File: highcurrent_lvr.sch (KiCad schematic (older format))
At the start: 6 parts

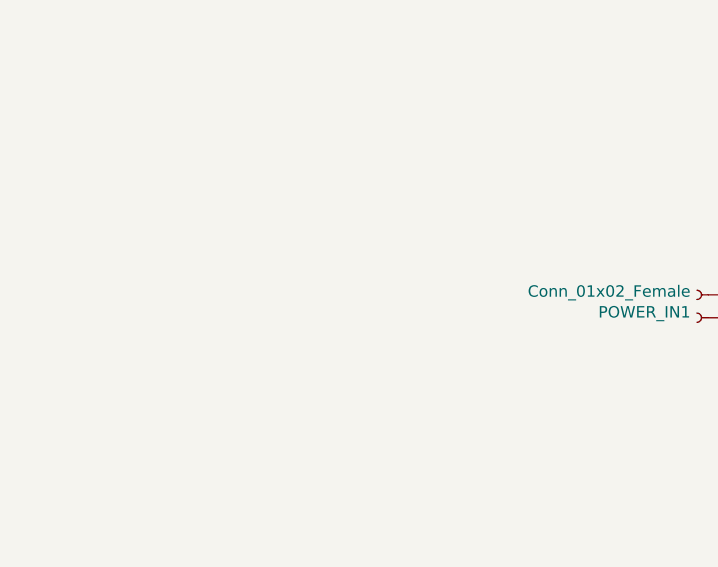
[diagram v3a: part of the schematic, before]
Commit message: added panelization
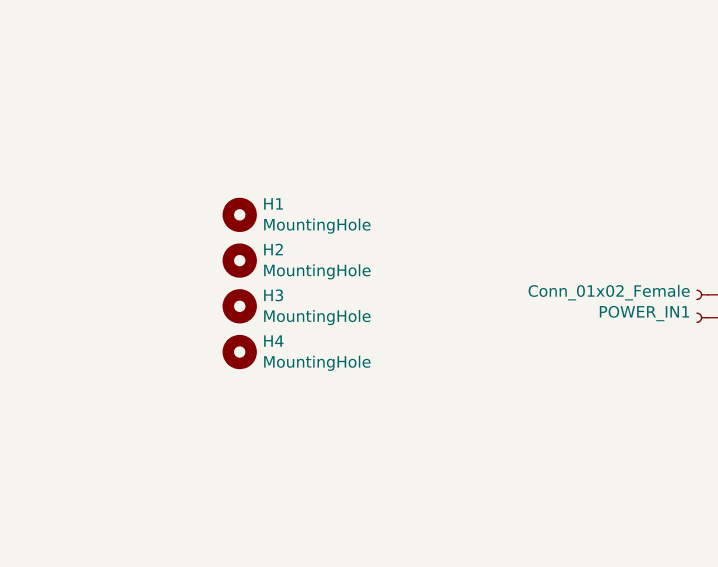
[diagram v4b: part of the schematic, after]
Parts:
- added H1, H2, H3, H4: MountingHole, MountingHole:MountingHole_4mm, symbol Mechanical:MountingHole
- POWER_IN1, POWER_OUT1: dk_pn 277-1258-ND -> (none); ms_pn 651-1711026 -> (none)
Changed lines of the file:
@@
 Text Notes 3750 4600 0    50   ~ 0
 add reverse polarity protection
-$Comp
-L Connector:Conn_01x02_Female POWER_IN1
-U 1 1 602E4815
-P 3550 3250
-F 0 "POWER_IN1" H 3578 3226 50  0000 L CNN
-F 1 "Conn_01x02_Female" H 3578 3135 50  0000 L CNN
-F 2 "wire-connector-lib:connector-wire-3cm2-2pin-smd" H 3550 3250 50  0001 C CNN
-F 3 "~" H 3550 3250 50  0001 C CNN
-F 4 "651-1711026" H 3550 3250 50  0001 C CNN "ms_pn"
-F 5 "277-1258-ND" H 3550 3250 50  0001 C CNN "dk_pn"
-	1    3550 3250
-	-1   0    0    1
-$EndComp
-$Comp
-L Connector:Conn_01x02_Female POWER_OUT1
-U 1 1 602E8D12
-P 8150 3250
-F 0 "POWER_OUT1" H 8178 3226 50  0000 L CNN
-F 1 "Conn_01x02_Female" H 8178 3135 50  0000 L CNN
-F 2 "wire-connector-lib:connector-wire-3cm2-2pin-smd" H 8150 3250 50  0001 C CNN
-F 3 "~" H 8150 3250 50  0001 C CNN
-F 4 "651-1711026" H 8150 3250 50  0001 C CNN "ms_pn"
-F 5 "277-1258-ND" H 8150 3250 50  0001 C CNN "dk_pn"
-	1    8150 3250
-	1    0    0    1
-$EndComp
-$Comp
-L Device:LED D1
-U 1 1 60393075
-P 7250 4150
-F 0 "D1" V 7289 4032 50  0000 R CNN
-F 1 "LED" V 7198 4032 50  0000 R CNN
-F 2 "LED_SMD:LED_0805_2012Metric_Pad1.15x1.40mm_HandSolder" H 7250 4150 50  0001 C CNN
-F 3 "~" H 7250 4150 50  0001 C CNN
-F 4 "754-2044-1-ND" H 7250 4150 50  0001 C CNN "dk_pn"
-F 5 "604-APTD2012LSURCK" H 7250 4150 50  0001 C CNN "ms_pn"
-	1    7250 4150
-	0    -1   -1   0
-$EndComp
 Wire Wire Line
 	7250 3450 7250 4000
-$Comp
-L Device:R R7
-U 1 1 603954F6
-P 7250 4600
-F 0 "R7" H 7320 4646 50  0000 L CNN
-F 1 "1k8" H 7320 4555 50  0000 L CNN
-F 2 "Resistor_SMD:R_0805_2012Metric_Pad1.20x1.40mm_HandSolder" V 7180 4600 50  0001 C CNN
-F 3 "~" H 7250 4600 50  0001 C CNN
-F 4 "541-10510-1-ND" H 7250 4600 50  0001 C CNN "dk_pn"
-F 5 "71-RCS08051K80FKEA" H 7250 4600 50  0001 C CNN "ms_pn"
-	1    7250 4600
-	1    0    0    -1
-$EndComp
 $Comp
 L power:GND #PWR0108
@@
 Wire Wire Line
 	7250 4450 7250 4300
-$Comp
-L Device:LED D2
-U 1 1 603BAE9B
-P 5450 4100
-F 0 "D2" V 5489 3982 50  0000 R CNN
-F 1 "LED" V 5398 3982 50  0000 R CNN
-F 2 "LED_SMD:LED_0805_2012Metric_Pad1.15x1.40mm_HandSolder" H 5450 4100 50  0001 C CNN
-F 3 "~" H 5450 4100 50  0001 C CNN
-F 4 "754-2044-1-ND" H 5450 4100 50  0001 C CNN "dk_pn"
-F 5 "604-APTD2012LSURCK" H 5450 4100 50  0001 C CNN "ms_pn"
-	1    5450 4100
-	0    -1   -1   0
-$EndComp
-$Comp
-L Device:R R6
-U 1 1 603BAEA3
-P 5450 4550
-F 0 "R6" H 5520 4596 50  0000 L CNN
-F 1 "1k8" H 5520 4505 50  0000 L CNN
-F 2 "Resistor_SMD:R_0805_2012Metric_Pad1.20x1.40mm_HandSolder" V 5380 4550 50  0001 C CNN
-F 3 "~" H 5450 4550 50  0001 C CNN
-F 4 "541-10510-1-ND" H 5450 4550 50  0001 C CNN "dk_pn"
-F 5 "71-RCS08051K80FKEA" H 5450 4550 50  0001 C CNN "ms_pn"
-	1    5450 4550
-	1    0    0    -1
-$EndComp
 $Comp
 L power:GND #PWR0114
@@
 Wire Wire Line
 	7100 3150 7950 3150
+$Comp
+L Device:R R6
+U 1 1 603BAEA3
+P 5450 4550
+F 0 "R6" H 5520 4596 50  0000 L CNN
+F 1 "1k8" H 5520 4505 50  0000 L CNN
+F 2 "Resistor_SMD:R_0805_2012Metric_Pad1.20x1.40mm_HandSolder" V 5380 4550 50  0001 C CNN
+F 3 "~" H 5450 4550 50  0001 C CNN
+F 4 "541-10510-1-ND" H 5450 4550 50  0001 C CNN "dk_pn"
+F 5 "71-RCS08051K80FKEA" H 5450 4550 50  0001 C CNN "ms_pn"
+	1    5450 4550
+	1    0    0    -1
+$EndComp
+$Comp
+L Device:LED D2
+U 1 1 603BAE9B
+P 5450 4100
+F 0 "D2" V 5489 3982 50  0000 R CNN
+F 1 "LED" V 5398 3982 50  0000 R CNN
+F 2 "LED_SMD:LED_0805_2012Metric_Pad1.15x1.40mm_HandSolder" H 5450 4100 50  0001 C CNN
+F 3 "~" H 5450 4100 50  0001 C CNN
+F 4 "754-2044-1-ND" H 5450 4100 50  0001 C CNN "dk_pn"
+F 5 "604-APTD2012LSURCK" H 5450 4100 50  0001 C CNN "ms_pn"
+	1    5450 4100
+	0    -1   -1   0
+$EndComp
+$Comp
+L Device:R R7
+U 1 1 603954F6
+P 7250 4600
+F 0 "R7" H 7320 4646 50  0000 L CNN
+F 1 "1k8" H 7320 4555 50  0000 L CNN
+F 2 "Resistor_SMD:R_0805_2012Metric_Pad1.20x1.40mm_HandSolder" V 7180 4600 50  0001 C CNN
+F 3 "~" H 7250 4600 50  0001 C CNN
+F 4 "541-10510-1-ND" H 7250 4600 50  0001 C CNN "dk_pn"
+F 5 "71-RCS08051K80FKEA" H 7250 4600 50  0001 C CNN "ms_pn"
+	1    7250 4600
+	1    0    0    -1
+$EndComp
+$Comp
+L Device:LED D1
+U 1 1 60393075
+P 7250 4150
+F 0 "D1" V 7289 4032 50  0000 R CNN
+F 1 "LED" V 7198 4032 50  0000 R CNN
+F 2 "LED_SMD:LED_0805_2012Metric_Pad1.15x1.40mm_HandSolder" H 7250 4150 50  0001 C CNN
+F 3 "~" H 7250 4150 50  0001 C CNN
+F 4 "754-2044-1-ND" H 7250 4150 50  0001 C CNN "dk_pn"
+F 5 "604-APTD2012LSURCK" H 7250 4150 50  0001 C CNN "ms_pn"
+	1    7250 4150
+	0    -1   -1   0
+$EndComp
+$Comp
+L Connector:Conn_01x02_Female POWER_OUT1
+U 1 1 602E8D12
+P 8150 3250
+F 0 "POWER_OUT1" H 8178 3226 50  0000 L CNN
+F 1 "Conn_01x02_Female" H 8178 3135 50  0000 L CNN
+F 2 "wire-connector-lib:connector-wire-3cm2-2pin-smd" H 8150 3250 50  0001 C CNN
+F 3 "~" H 8150 3250 50  0001 C CNN
+F 4 "" H 8150 3250 50  0001 C CNN "ms_pn"
+F 5 "" H 8150 3250 50  0001 C CNN "dk_pn"
+	1    8150 3250
+	1    0    0    1
+$EndComp
+$Comp
+L Connector:Conn_01x02_Female POWER_IN1
+U 1 1 602E4815
+P 3550 3250
+F 0 "POWER_IN1" H 3578 3226 50  0000 L CNN
+F 1 "Conn_01x02_Female" H 3578 3135 50  0000 L CNN
+F 2 "wire-connector-lib:connector-wire-3cm2-2pin-smd" H 3550 3250 50  0001 C CNN
+F 3 "~" H 3550 3250 50  0001 C CNN
+F 4 "" H 3550 3250 50  0001 C CNN "ms_pn"
+F 5 "" H 3550 3250 50  0001 C CNN "dk_pn"
+	1    3550 3250
+	-1   0    0    1
+$EndComp
+$Comp
+L Mechanical:MountingHole H4
+U 1 1 603CCF38
+P 1550 3400
+F 0 "H4" H 1650 3446 50  0000 L CNN
+F 1 "MountingHole" H 1650 3355 50  0000 L CNN
+F 2 "MountingHole:MountingHole_4mm" H 1550 3400 50  0001 C CNN
+F 3 "~" H 1550 3400 50  0001 C CNN
+	1    1550 3400
+	1    0    0    -1
+$EndComp
+$Comp
+L Mechanical:MountingHole H3
+U 1 1 603CCCAE
+P 1550 3200
+F 0 "H3" H 1650 3246 50  0000 L CNN
+F 1 "MountingHole" H 1650 3155 50  0000 L CNN
+F 2 "MountingHole:MountingHole_4mm" H 1550 3200 50  0001 C CNN
+F 3 "~" H 1550 3200 50  0001 C CNN
+	1    1550 3200
+	1    0    0    -1
+$EndComp
+$Comp
+L Mechanical:MountingHole H2
+U 1 1 603CCA44
+P 1550 3000
+F 0 "H2" H 1650 3046 50  0000 L CNN
+F 1 "MountingHole" H 1650 2955 50  0000 L CNN
+F 2 "MountingHole:MountingHole_4mm" H 1550 3000 50  0001 C CNN
+F 3 "~" H 1550 3000 50  0001 C CNN
+	1    1550 3000
+	1    0    0    -1
+$EndComp
+$Comp
+L Mechanical:MountingHole H1
+U 1 1 603CA106
+P 1550 2800
+F 0 "H1" H 1650 2846 50  0000 L CNN
+F 1 "MountingHole" H 1650 2755 50  0000 L CNN
+F 2 "MountingHole:MountingHole_4mm" H 1550 2800 50  0001 C CNN
+F 3 "~" H 1550 2800 50  0001 C CNN
+	1    1550 2800
+	1    0    0    -1
+$EndComp
 $EndSCHEMATC
